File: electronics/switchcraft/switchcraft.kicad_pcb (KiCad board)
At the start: 2 copper layers, 90 x 89.7 mm, 69 parts, among them Q10 BC548, Q11 BC548, Q12 BC548, Q13 BC548, Q14 BC559, Q3 BC559, Q4 BC548, Q5 BC548, Q6 BC548, Q7 BC548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

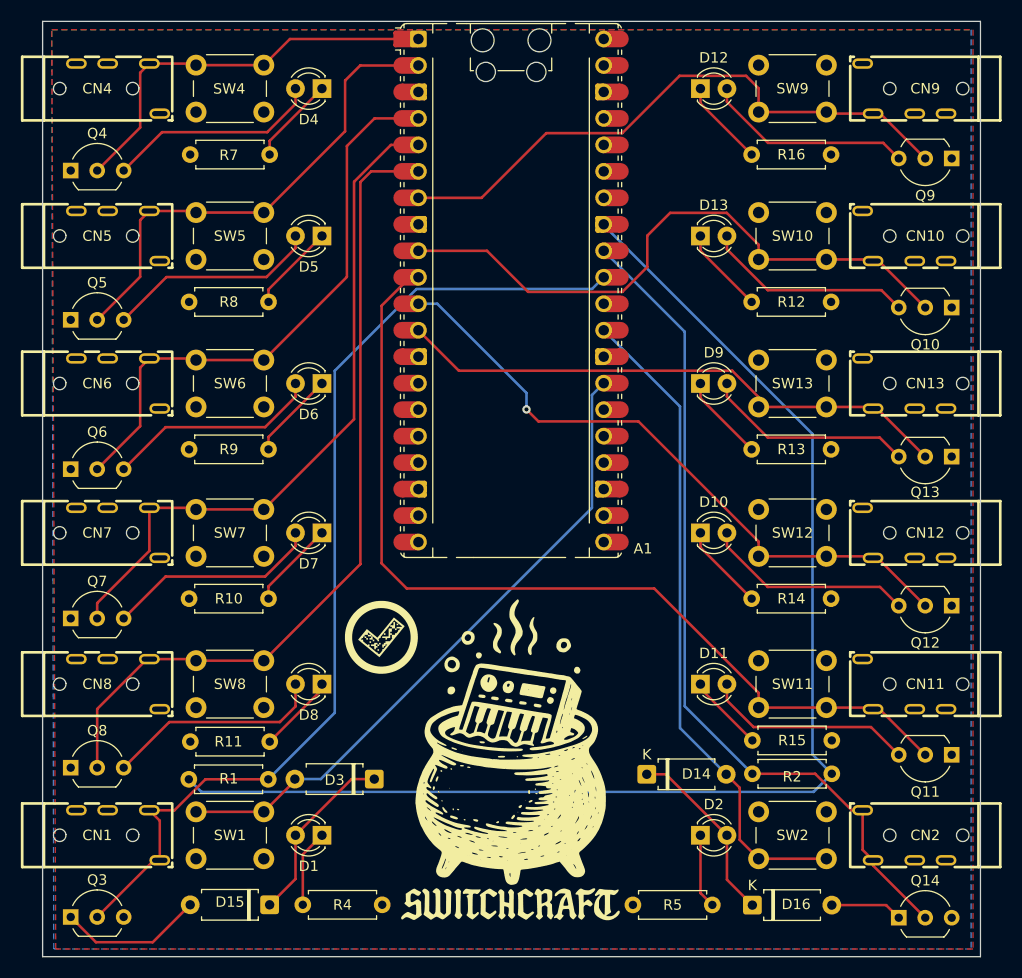
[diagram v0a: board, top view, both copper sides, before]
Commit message: simplified continuous inputs
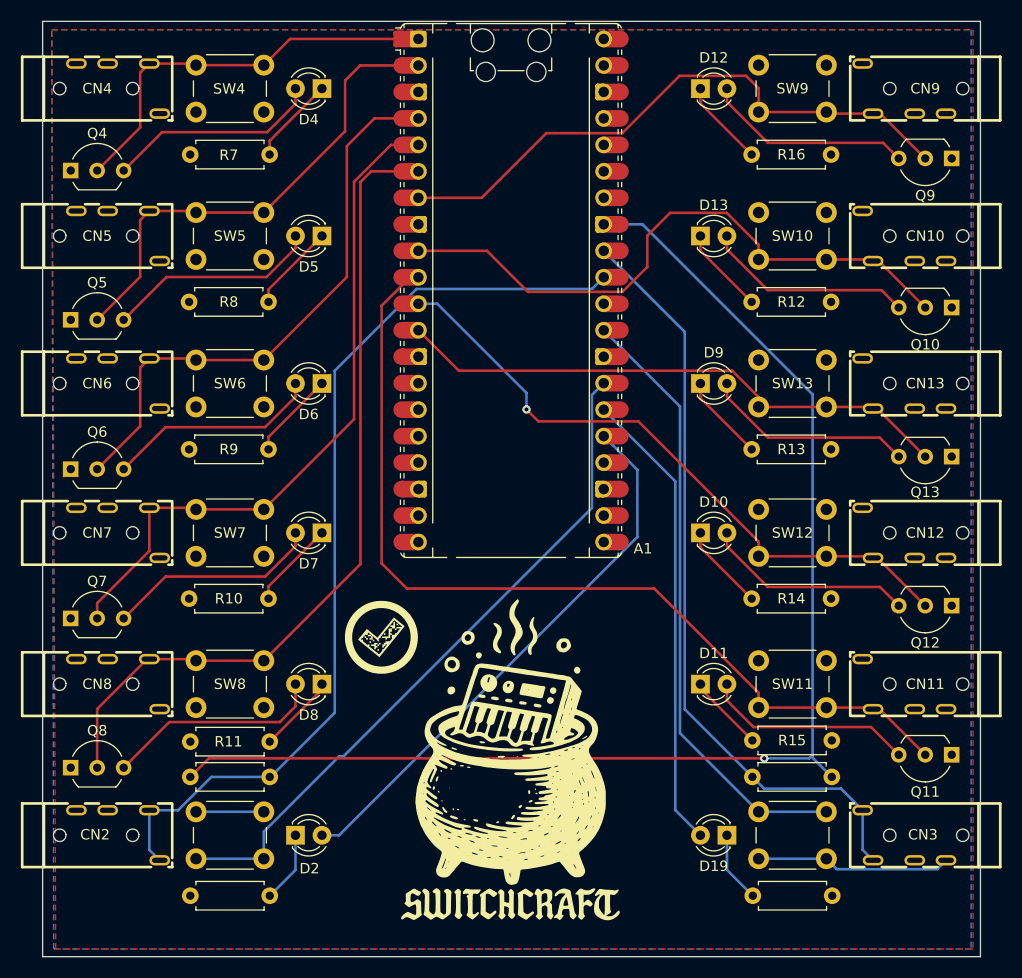
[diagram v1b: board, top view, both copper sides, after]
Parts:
- removed CN1: ~, ng:PJ-320A
- removed D1: LED, LED_THT:LED_D3.0mm
- removed D14, D15, D16, D3: D, Diode_THT:D_A-405_P7.62mm_Horizontal
- removed Q14, Q3: BC559, Package_TO_SOT_THT:TO-92_Inline_Wide
- removed R1: 10K, Resistor_THT:R_Axial_DIN0207_L6.3mm_D2.5mm_P7.62mm_Horizontal
- removed R4: 62r, Resistor_THT:R_Axial_DIN0207_L6.3mm_D2.5mm_P7.62mm_Horizontal
- removed SW1: SW_Push, Button_Switch_THT:SW_PUSH_6mm
- added CN3: ~, ng:PJ-320A, F.Cu at (177.9, 135.0)
- added D19: LED, LED_THT:LED_D3.0mm, F.Cu at (160.9, 135.0)
- added R3: 10K, Resistor_THT:R_Axial_DIN0207_L6.3mm_D2.5mm_P7.62mm_Horizontal, F.Cu at (163.3, 129.4)
- added R6: 62r, Resistor_THT:R_Axial_DIN0207_L6.3mm_D2.5mm_P7.62mm_Horizontal, F.Cu at (163.4, 140.8)
- added SW3: SW_Push, Button_Switch_THT:SW_PUSH_6mm, F.Cu at (170.4, 137.2)
- moved CN2 75.4 mm to (102.5, 135.0), turned to 0 degrees
- moved SW2 60.6 mm to (110.0, 132.8), turned to 0 degrees
- moved R2 46.3 mm to (117.0, 129.4), turned to 180 degrees
- moved R5 42.5 mm to (117.0, 140.8)
- moved D2 38.9 mm to (119.5, 135.0)
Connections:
- A1 pad 25: unconnected-(A1-GPIO19-Pad25) -> /new_continuous1/GPIO_LED
- A1 pad 26: unconnected-(A1-GPIO20-Pad26) -> /new_continuous/GPIO_LED
- A1 pad 27: /continuous_input/GPIO -> /new_continuous1/GPIO_BUTTON
- A1 pad 29: /continuous_input1/GPIO -> /new_continuous/GPIO_BUTTON
- A1 pad 31: /continuous_input/ADC -> /new_continuous1/ADC
- A1 pad 32: /continuous_input1/ADC -> /new_continuous/ADC
- CN2 pad 4: /continuous_input1/ADC -> /new_continuous1/ADC
- CN2 pad 5: /continuous_input1/ADC -> /new_continuous1/ADC
- D2 pad 2: Net-(D14-K) -> /new_continuous1/GPIO_LED
- R2 pad 1: /continuous_input1/ADC -> /new_continuous1/ADC
- SW2 pad 1: /continuous_input1/GPIO -> +3V3
- SW2 pad 2: +3V3 -> /new_continuous1/GPIO_BUTTON
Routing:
- net /continuous_input/ADC: track 97.5 -> 0.00 mm
- net /new_continuous1/ADC: track 0.00 -> 89.4 mm
- net /continuous_input1/ADC: track 80.9 -> 0.00 mm
- net /new_continuous/ADC: track 0.00 -> 73.5 mm
- net /new_continuous1/GPIO_BUTTON: track 0.00 -> 65.9 mm
- net /continuous_input1/GPIO: track 63.4 -> 0.00 mm
- net /continuous_input/GPIO: track 62.6 -> 0.00 mm
- net /new_continuous/GPIO_BUTTON: track 0.00 -> 58.9 mm
- net /new_continuous1/GPIO_LED: track 0.00 -> 53.1 mm
- net /new_continuous/GPIO_LED: track 0.00 -> 44.7 mm
- net +3V3: track 0.00 -> 25.2 mm
- net Net-(D14-K): track 17.8 -> 0.00 mm
- net Net-(D1-A): track 17.5 -> 0.00 mm
- net Net-(D15-A): track 14.0 -> 0.00 mm
- net Net-(D1-K): track 7.43 -> 0.00 mm
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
